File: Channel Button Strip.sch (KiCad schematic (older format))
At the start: 13 parts, among them J3 Conn_01x08_Male, J4 Conn_01x01_Male, J5 Conn_01x01_Male, J6 Conn_01x01_Male, J7 Conn_01x01_Male, SW33 SW_SPST_4_PIN, SW34 SW_SPST_4_PIN, SW35 SW_SPST_4_PIN, SW36 SW_SPST_4_PIN, SW37 SW_SPST_4_PIN, SW38 SW_SPST_4_PIN, SW39 SW_SPST_4_PIN, SW40 SW_SPST_4_PIN

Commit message: Further work on the separate boards
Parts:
- SW33, SW34, SW35, SW36, SW37, SW38, SW39, SW40: symbol sw_spst_0:SW_SPST_4_PIN -> cp_midi_control_surface_002-rescue:SW_SPST_4_PIN-sw_spst_0
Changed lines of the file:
@@
 $EndDescr
 $Comp
-L sw_spst_0:SW_SPST_4_PIN SW?
+L cp_midi_control_surface_002-rescue:SW_SPST_4_PIN-sw_spst_0 SW?
 U 1 1 5C4BA780
 P 2750 1900
 AR Path="/5C4B73B3/5C4BA780" Ref="SW?"  Part="1"
 AR Path="/5C4BA289/5C4BA780" Ref="SW33"  Part="1"
+AR Path="/5C4BA780" Ref="SW33"  Part="1"
 F 0 "SW33" H 2750 1700 50  0000 C CNN
 F 1 "SW_SPST_4_PIN" H 2750 2074 50  0001 C CNN
@@
 $EndComp
 $Comp
-L sw_spst_0:SW_SPST_4_PIN SW?
+L cp_midi_control_surface_002-rescue:SW_SPST_4_PIN-sw_spst_0 SW?
 U 1 1 5C4BA787
 P 2750 2400
 AR Path="/5C4B73B3/5C4BA787" Ref="SW?"  Part="1"
 AR Path="/5C4BA289/5C4BA787" Ref="SW34"  Part="1"
+AR Path="/5C4BA787" Ref="SW34"  Part="1"
 F 0 "SW34" H 2750 2200 50  0000 C CNN
 F 1 "SW_SPST_4_PIN" H 2750 2574 50  0001 C CNN
@@
 $EndComp
 $Comp
-L sw_spst_0:SW_SPST_4_PIN SW?
+L cp_midi_control_surface_002-rescue:SW_SPST_4_PIN-sw_spst_0 SW?
 U 1 1 5C4BA78E
 P 2750 2900
 AR Path="/5C4B73B3/5C4BA78E" Ref="SW?"  Part="1"
 AR Path="/5C4BA289/5C4BA78E" Ref="SW35"  Part="1"
+AR Path="/5C4BA78E" Ref="SW35"  Part="1"
 F 0 "SW35" H 2750 2700 50  0000 C CNN
 F 1 "SW_SPST_4_PIN" H 2750 3074 50  0001 C CNN
@@
 $EndComp
 $Comp
-L sw_spst_0:SW_SPST_4_PIN SW?
+L cp_midi_control_surface_002-rescue:SW_SPST_4_PIN-sw_spst_0 SW?
 U 1 1 5C4BA795
 P 2750 3400
 AR Path="/5C4B73B3/5C4BA795" Ref="SW?"  Part="1"
 AR Path="/5C4BA289/5C4BA795" Ref="SW36"  Part="1"
+AR Path="/5C4BA795" Ref="SW36"  Part="1"
 F 0 "SW36" H 2750 3200 50  0000 C CNN
 F 1 "SW_SPST_4_PIN" H 2750 3574 50  0001 C CNN
@@
 $EndComp
 $Comp
-L sw_spst_0:SW_SPST_4_PIN SW?
+L cp_midi_control_surface_002-rescue:SW_SPST_4_PIN-sw_spst_0 SW?
 U 1 1 5C4BA79C
 P 2750 3900
 AR Path="/5C4B73B3/5C4BA79C" Ref="SW?"  Part="1"
 AR Path="/5C4BA289/5C4BA79C" Ref="SW37"  Part="1"
+AR Path="/5C4BA79C" Ref="SW37"  Part="1"
 F 0 "SW37" H 2750 3700 50  0000 C CNN
 F 1 "SW_SPST_4_PIN" H 2750 4074 50  0001 C CNN
@@
 $EndComp
 $Comp
-L sw_spst_0:SW_SPST_4_PIN SW?
+L cp_midi_control_surface_002-rescue:SW_SPST_4_PIN-sw_spst_0 SW?
 U 1 1 5C4BA7A3
 P 2750 4400
 AR Path="/5C4B73B3/5C4BA7A3" Ref="SW?"  Part="1"
 AR Path="/5C4BA289/5C4BA7A3" Ref="SW38"  Part="1"
+AR Path="/5C4BA7A3" Ref="SW38"  Part="1"
 F 0 "SW38" H 2750 4200 50  0000 C CNN
 F 1 "SW_SPST_4_PIN" H 2750 4574 50  0001 C CNN
@@
 $EndComp
 $Comp
-L sw_spst_0:SW_SPST_4_PIN SW?
+L cp_midi_control_surface_002-rescue:SW_SPST_4_PIN-sw_spst_0 SW?
 U 1 1 5C4BA7AA
 P 2750 4900
 AR Path="/5C4B73B3/5C4BA7AA" Ref="SW?"  Part="1"
 AR Path="/5C4BA289/5C4BA7AA" Ref="SW39"  Part="1"
+AR Path="/5C4BA7AA" Ref="SW39"  Part="1"
 F 0 "SW39" H 2750 4700 50  0000 C CNN
 F 1 "SW_SPST_4_PIN" H 2750 5074 50  0001 C CNN
@@
 $EndComp
 $Comp
-L sw_spst_0:SW_SPST_4_PIN SW?
+L cp_midi_control_surface_002-rescue:SW_SPST_4_PIN-sw_spst_0 SW?
 U 1 1 5C4BA7B1
 P 2750 5400
 AR Path="/5C4B73B3/5C4BA7B1" Ref="SW?"  Part="1"
 AR Path="/5C4BA289/5C4BA7B1" Ref="SW40"  Part="1"
+AR Path="/5C4BA7B1" Ref="SW40"  Part="1"
 F 0 "SW40" H 2750 5200 50  0000 C CNN
 F 1 "SW_SPST_4_PIN" H 2750 5574 50  0001 C CNN

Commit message: Sub boards completed
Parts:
- removed J3: Conn_01x08_Male, Connector_PinHeader_2.54mm:PinHeader_1x08_P2.54mm_Vertical, symbol Connector:Conn_01x08_Male
- added J24, J3: Conn_01x04_Male, Connector_PinHeader_2.54mm:PinHeader_1x04_P2.54mm_Vertical, symbol Connector:Conn_01x04_Male
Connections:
- net at SW33.1 (A): now also J3.1 (Pin_1)
- net at SW34.1 (A): now also J3.2 (Pin_2)
- net at SW35.1 (A): now also J3.3 (Pin_3)
- net at SW36.1 (A): now also J3.4 (Pin_4)
- net B_CHAN_1: no longer names the net of SW33.2
- net B_CHAN_2: no longer names the net of SW34.2
- net B_CHAN_3: no longer names the net of SW35.2
- net B_CHAN_4: no longer names the net of SW36.2
- net B_CHAN_5: no longer names the net of SW37.1 (A)
- net B_CHAN_5: now also J24.1 (Pin_1)
- net B_CHAN_6: no longer names the net of SW38.1 (A)
- net B_CHAN_6: now also J24.2 (Pin_2)
- net B_CHAN_7: no longer names the net of SW39.1 (A)
- net B_CHAN_7: now also J24.3 (Pin_3)
- net B_CHAN_8: no longer names the net of SW40.1 (A)
- net B_CHAN_8: now also J24.4 (Pin_4)
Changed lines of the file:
@@
 Wire Wire Line
 	3100 2400 3100 2900
-Text HLabel 2350 2000 0    50   Input ~ 0
-B_CHAN_1
-Text HLabel 2350 2500 0    50   Input ~ 0
-B_CHAN_2
-Text HLabel 2350 3000 0    50   Input ~ 0
-B_CHAN_3
-Text HLabel 2350 3500 0    50   Input ~ 0
-B_CHAN_4
-Text HLabel 2350 3900 0    50   Input ~ 0
-B_CHAN_5
-Text HLabel 2350 4400 0    50   Input ~ 0
-B_CHAN_6
-Text HLabel 2350 4900 0    50   Input ~ 0
-B_CHAN_7
-Text HLabel 2350 5400 0    50   Input ~ 0
-B_CHAN_8
-Wire Wire Line
-	2350 2000 2450 2000
-Wire Wire Line
-	2350 2500 2450 2500
-Wire Wire Line
-	2350 3000 2450 3000
-Wire Wire Line
-	2350 3500 2450 3500
-Wire Wire Line
-	2350 3900 2450 3900
-Wire Wire Line
-	2350 4400 2450 4400
-Wire Wire Line
-	2350 4900 2450 4900
-Wire Wire Line
-	2350 5400 2450 5400
 NoConn ~ 2950 2000
 NoConn ~ 2950 2500
@@
 NoConn ~ 2550 5500
 NoConn ~ 2950 5500
-NoConn ~ 2550 1900
-NoConn ~ 2550 2400
-NoConn ~ 2550 2900
-NoConn ~ 2550 3400
-$Comp
-L Connector:Conn_01x08_Male J3
-U 1 1 5CBFD5BE
-P 650 2400
-F 0 "J3" H 756 2878 50  0000 C CNN
-F 1 "Conn_01x08_Male" H 756 2787 50  0000 C CNN
-F 2 "Connector_PinHeader_2.54mm:PinHeader_1x08_P2.54mm_Vertical" H 650 2400 50  0001 C CNN
-F 3 "~" H 650 2400 50  0001 C CNN
-	1    650  2400
-	1    0    0    -1
-$EndComp
-Wire Wire Line
-	2450 2000 2450 2100
-Wire Wire Line
-	2450 2100 850  2100
-Connection ~ 2450 2000
-Wire Wire Line
-	2450 2000 2550 2000
-Wire Wire Line
-	2450 2500 2450 2600
-Wire Wire Line
-	2450 2600 1850 2600
-Wire Wire Line
-	1850 2600 1850 2200
-Wire Wire Line
-	1850 2200 850  2200
-Connection ~ 2450 2500
-Wire Wire Line
-	2450 2500 2550 2500
-Wire Wire Line
-	850  2300 1750 2300
-Wire Wire Line
-	1750 2300 1750 3100
-Wire Wire Line
-	1750 3100 2450 3100
-Wire Wire Line
-	2450 3100 2450 3000
-Connection ~ 2450 3000
-Wire Wire Line
-	2450 3000 2550 3000
-Wire Wire Line
-	850  2400 1650 2400
-Wire Wire Line
-	1650 2400 1650 3600
-Wire Wire Line
-	1650 3600 2450 3600
-Wire Wire Line
-	2450 3600 2450 3500
-Connection ~ 2450 3500
-Wire Wire Line
-	2450 3500 2550 3500
-Wire Wire Line
-	850  2500 1550 2500
-Wire Wire Line
-	1550 2500 1550 4000
-Wire Wire Line
-	1550 4000 2450 4000
-Wire Wire Line
-	2450 4000 2450 3900
-Connection ~ 2450 3900
-Wire Wire Line
-	2450 3900 2550 3900
-Wire Wire Line
-	850  2600 1450 2600
-Wire Wire Line
-	1450 2600 1450 4500
-Wire Wire Line
-	1450 4500 2450 4500
-Wire Wire Line
-	2450 4500 2450 4400
-Connection ~ 2450 4400
-Wire Wire Line
-	2450 4400 2550 4400
-Wire Wire Line
-	850  2700 1350 2700
-Wire Wire Line
-	1350 2700 1350 5000
-Wire Wire Line
-	1350 5000 2450 5000
-Wire Wire Line
-	2450 5000 2450 4900
-Connection ~ 2450 4900
-Wire Wire Line
-	2450 4900 2550 4900
-Wire Wire Line
-	850  2800 1250 2800
-Wire Wire Line
-	1250 2800 1250 5500
-Wire Wire Line
-	1250 5500 2450 5500
-Wire Wire Line
-	2450 5500 2450 5400
-Connection ~ 2450 5400
-Wire Wire Line
-	2450 5400 2550 5400
 $Comp
 L Connector:Conn_01x01_Male J7
@@
 	3100 6650 3100 6900
 Connection ~ 3100 6650
+$Comp
+L Connector:Conn_01x04_Male J3
+U 1 1 5C755D1C
+P 1950 2000
+F 0 "J3" H 2056 2278 50  0000 C CNN
+F 1 "Conn_01x04_Male" H 2056 2187 50  0000 C CNN
+F 2 "Connector_PinHeader_2.54mm:PinHeader_1x04_P2.54mm_Vertical" H 1950 2000 50  0001 C CNN
+F 3 "~" H 1950 2000 50  0001 C CNN
+	1    1950 2000
+	1    0    0    -1
+$EndComp
+$Comp
+L Connector:Conn_01x04_Male J24
+U 1 1 5C756AEE
+P 1950 4000
+F 0 "J24" H 2056 4278 50  0000 C CNN
+F 1 "Conn_01x04_Male" H 2056 4187 50  0000 C CNN
+F 2 "Connector_PinHeader_2.54mm:PinHeader_1x04_P2.54mm_Vertical" H 1950 4000 50  0001 C CNN
+F 3 "~" H 1950 4000 50  0001 C CNN
+	1    1950 4000
+	1    0    0    -1
+$EndComp
+Wire Wire Line
+	2550 4400 2450 4400
+Wire Wire Line
+	2450 4400 2450 4000
+Wire Wire Line
+	2550 4900 2350 4900
+Wire Wire Line
+	2350 4900 2350 4100
+Wire Wire Line
+	2550 5400 2250 5400
+Wire Wire Line
+	2250 5400 2250 4200
+Wire Wire Line
+	2250 4200 2150 4200
+Wire Wire Line
+	2350 4100 2150 4100
+Wire Wire Line
+	2450 4000 2150 4000
+Wire Wire Line
+	2550 3900 2150 3900
+Wire Wire Line
+	2550 1900 2150 1900
+Wire Wire Line
+	2550 2400 2450 2400
+Wire Wire Line
+	2450 2400 2450 2000
+Wire Wire Line
+	2450 2000 2150 2000
+Wire Wire Line
+	2550 2900 2350 2900
+Wire Wire Line
+	2350 2900 2350 2100
+Wire Wire Line
+	2350 2100 2150 2100
+Wire Wire Line
+	2550 3400 2250 3400
+Wire Wire Line
+	2250 3400 2250 2200
+Wire Wire Line
+	2250 2200 2150 2200
+NoConn ~ 2550 2000
+NoConn ~ 2550 2500
+NoConn ~ 2550 3000
+NoConn ~ 2550 3500
 $EndSCHEMATC

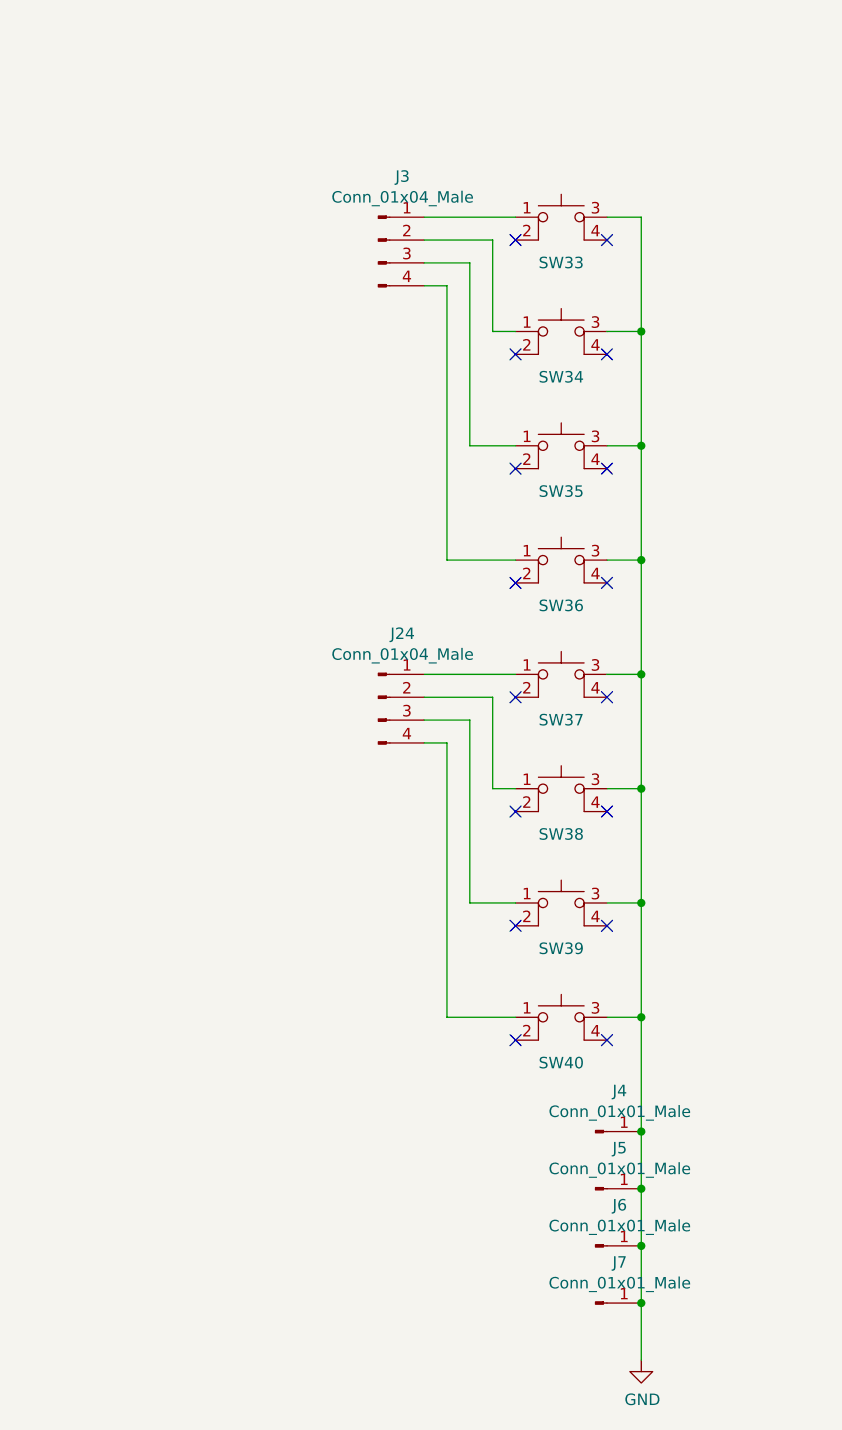
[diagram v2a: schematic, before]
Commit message: Tidy schematic / renumber components / complete daughter boards
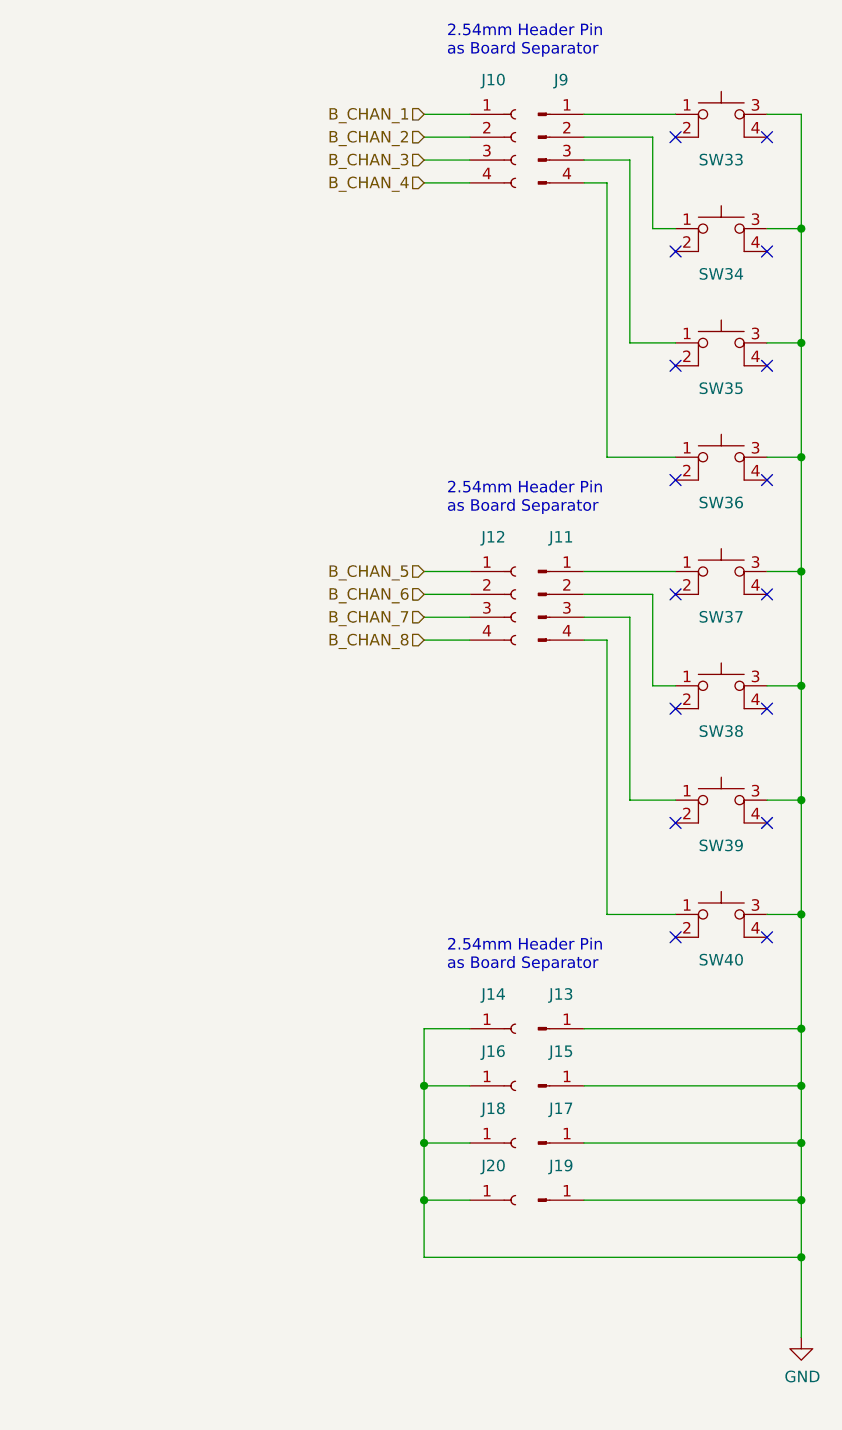
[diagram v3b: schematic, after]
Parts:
- added J10, J12: ~, Connector_PinSocket_2.54mm:PinSocket_1x04_P2.54mm_Vertical, symbol Connector:Conn_01x04_Female
- added J14, J16, J18, J20: ~, Connector_PinSocket_2.54mm:PinSocket_1x01_P2.54mm_Vertical, symbol Connector:Conn_01x01_Female
- J11: renamed from J24; value Conn_01x04_Male -> ~
- J13: renamed from J4; value Conn_01x01_Male -> ~
- J15: renamed from J5; value Conn_01x01_Male -> ~
- J17: renamed from J6; value Conn_01x01_Male -> ~
- J19: renamed from J7; value Conn_01x01_Male -> ~
- J9: renamed from J3; value Conn_01x04_Male -> ~
- SW33, SW34, SW35, SW36, SW37, SW38, SW39, SW40: value SW_SPST_4_PIN -> B3F-5050
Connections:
- net GND: now also J14.1 (Pin_1), J16.1 (Pin_1), J18.1 (Pin_1), J20.1 (Pin_1)
- new net B_CHAN_1: J10.1 (Pin_1)
- new net B_CHAN_2: J10.2 (Pin_2)
- new net B_CHAN_3: J10.3 (Pin_3)
- new net B_CHAN_4: J10.4 (Pin_4)
- new net B_CHAN_5: J12.1 (Pin_1)
- new net B_CHAN_6: J12.2 (Pin_2)
- new net B_CHAN_7: J12.3 (Pin_3)
- new net B_CHAN_8: J12.4 (Pin_4)
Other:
- note added: "2.54mm Header Pin\nas Board Separator"
- moved on the sheet: J11, J13, J15, J17, J19, J9, SW33, SW34, SW35, SW36, SW37, SW38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

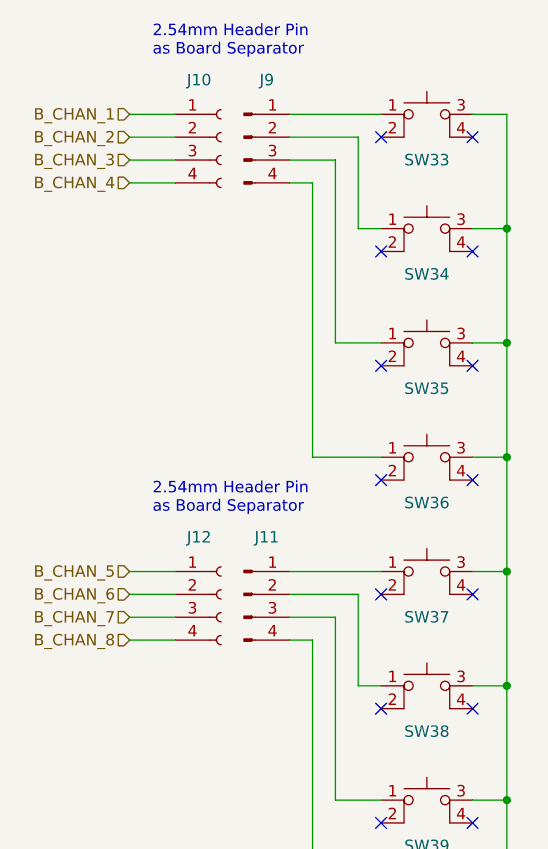
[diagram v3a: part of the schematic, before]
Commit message: More rerouting
Abortive try to reroute LEDs. Looked just as messy the other way round. Other general tidying.
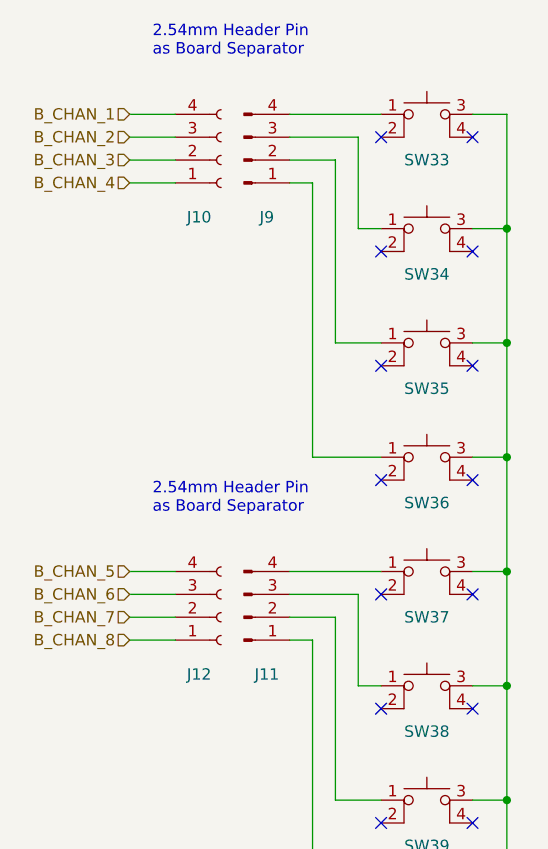
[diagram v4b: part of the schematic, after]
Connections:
- net B_CHAN_1: now also J10.4 (Pin_4); no longer J10.1 (Pin_1)
- net B_CHAN_2: now also J10.3 (Pin_3); no longer J10.2 (Pin_2)
- net B_CHAN_3: now also J10.2 (Pin_2); no longer J10.3 (Pin_3)
- net B_CHAN_4: now also J10.1 (Pin_1); no longer J10.4 (Pin_4)
- net B_CHAN_5: now also J12.4 (Pin_4); no longer J12.1 (Pin_1)
- net B_CHAN_6: now also J12.3 (Pin_3); no longer J12.2 (Pin_2)
- net B_CHAN_7: now also J12.2 (Pin_2); no longer J12.3 (Pin_3)
- net B_CHAN_8: now also J12.1 (Pin_1); no longer J12.4 (Pin_4)
- net at SW33.1 (A): now also J9.4 (Pin_4); no longer J9.1 (Pin_1)
- net at SW34.1 (A): now also J9.3 (Pin_3); no longer J9.2 (Pin_2)
- net at SW35.1 (A): now also J9.2 (Pin_2); no longer J9.3 (Pin_3)
- net at SW36.1 (A): now also J9.1 (Pin_1); no longer J9.4 (Pin_4)
- net at SW37.1 (A): now also J11.4 (Pin_4); no longer J11.1 (Pin_1)
- net at SW38.1 (A): now also J11.3 (Pin_3); no longer J11.2 (Pin_2)
- net at SW39.1 (A): now also J11.2 (Pin_2); no longer J11.3 (Pin_3)
- net at SW40.1 (A): now also J11.1 (Pin_1); no longer J11.4 (Pin_4)
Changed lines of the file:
@@
 L Connector:Conn_01x04_Male J9
 U 1 1 5C755D1C
-P 2650 1550
-F 0 "J9" H 2750 1800 50  0000 C CNN
-F 1 "~" H 2756 1737 50  0001 C CNN
-F 2 "Connector_PinHeader_2.54mm:PinHeader_1x04_P2.54mm_Vertical" H 2650 1550 50  0001 C CNN
-F 3 "~" H 2650 1550 50  0001 C CNN
-	1    2650 1550
-	1    0    0    -1
+P 2650 1650
+F 0 "J9" H 2750 1900 50  0000 C CNN
+F 1 "~" H 2756 1837 50  0001 C CNN
+F 2 "Connector_PinHeader_2.54mm:PinHeader_1x04_P2.54mm_Vertical" H 2650 1650 50  0001 C CNN
+F 3 "~" H 2650 1650 50  0001 C CNN
+	1    2650 1650
+	1    0    0    1
 $EndComp
 $Comp
 L Connector:Conn_01x04_Male J11
 U 1 1 5C756AEE
-P 2650 3550
-F 0 "J11" H 2750 3800 50  0000 C CNN
-F 1 "~" H 2756 3737 50  0001 C CNN
-F 2 "Connector_PinHeader_2.54mm:PinHeader_1x04_P2.54mm_Vertical" H 2650 3550 50  0001 C CNN
-F 3 "~" H 2650 3550 50  0001 C CNN
-	1    2650 3550
-	1    0    0    -1
+P 2650 3650
+F 0 "J11" H 2750 3900 50  0000 C CNN
+F 1 "~" H 2756 3837 50  0001 C CNN
+F 2 "Connector_PinHeader_2.54mm:PinHeader_1x04_P2.54mm_Vertical" H 2650 3650 50  0001 C CNN
+F 3 "~" H 2650 3650 50  0001 C CNN
+	1    2650 3650
+	1    0    0    1
 $EndComp
 Wire Wire Line
@@
 L Connector:Conn_01x04_Female J12
 U 1 1 5C8AD7FA
-P 2550 3550
-F 0 "J12" H 2400 3800 50  0000 L CNN
-F 1 "~" H 2577 3435 50  0001 L CNN
-F 2 "Connector_PinSocket_2.54mm:PinSocket_1x04_P2.54mm_Vertical" H 2550 3550 50  0001 C CNN
-F 3 "~" H 2550 3550 50  0001 C CNN
-	1    2550 3550
-	1    0    0    -1
+P 2550 3650
+F 0 "J12" H 2400 3900 50  0000 L CNN
+F 1 "~" H 2577 3535 50  0001 L CNN
+F 2 "Connector_PinSocket_2.54mm:PinSocket_1x04_P2.54mm_Vertical" H 2550 3650 50  0001 C CNN
+F 3 "~" H 2550 3650 50  0001 C CNN
+	1    2550 3650
+	1    0    0    1
 $EndComp
 $Comp
 L Connector:Conn_01x04_Female J10
 U 1 1 5C8ADE36
-P 2550 1550
-F 0 "J10" H 2400 1800 50  0000 L CNN
-F 1 "~" H 2577 1435 50  0001 L CNN
-F 2 "Connector_PinSocket_2.54mm:PinSocket_1x04_P2.54mm_Vertical" H 2550 1550 50  0001 C CNN
-F 3 "~" H 2550 1550 50  0001 C CNN
-	1    2550 1550
-	1    0    0    -1
+P 2550 1650
+F 0 "J10" H 2400 1900 50  0000 L CNN
+F 1 "~" H 2577 1535 50  0001 L CNN
+F 2 "Connector_PinSocket_2.54mm:PinSocket_1x04_P2.54mm_Vertical" H 2550 1650 50  0001 C CNN
+F 3 "~" H 2550 1650 50  0001 C CNN
+	1    2550 1650
+	1    0    0    1
 $EndComp
 Text HLabel 2150 1450 0    50   Input ~ 0
